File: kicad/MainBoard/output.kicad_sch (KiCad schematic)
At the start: 124 parts, among them J11 CHAN1, J12 CHAN2, J13 Conn_01x02, J14 CHAN3, J15 CHAN4, Q10 AO3400A, Q11 AO3400A, Q12 IRF9Z24NPBF, Q13 AO3400A, Q18 AO3401A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

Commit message: update out of stock 0.5R resistor C705591 to be C175573 instead
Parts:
- R36, R61: LCSC C705591 -> C175573
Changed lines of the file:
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@@
       (effects (font (size 1.27 1.27)) hide)
     )
-    (property "LCSC" "C705591" (id 4) (at 105.41 109.855 90)
+    (property "LCSC" "C175573" (id 4) (at 105.41 109.855 90)
       (effects (font (size 1.27 1.27)) hide)
     )
@@
       (effects (font (size 1.27 1.27)) hide)
     )
-    (property "LCSC" "C705591" (id 4) (at 105.41 17.145 90)
-      (effects (font (size 1.27 1.27)) hide)
-    )
+    (property "LCSC" "C175573" (id 4) (at 105.41 17.145 90)
+      (effects (font (size 1.27 1.27)) hide)
+    )

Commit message: Add PCB v2.3 kicad project files + gerbers
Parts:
- J13: footprint Connector_PinHeader_2.54mm:PinHeader_1x02_P2.54mm_Vertical -> Connector_Molex:Molex_KK-254_AE-6410-02A_1x02_P2.54mm_Vertical
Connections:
- net GND: now also J13.2 (Pin_2); no longer J13.1 (Pin_1)
- net SERIAL_TX: now also J13.1 (Pin_1); no longer J13.2 (Pin_2)
- net 4v renamed 3.5v
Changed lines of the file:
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@@
   (junction (at 128.27 180.975) (diameter 0) (color 0 0 0 0)
   )
+  (junction (at 84.455 210.185) (diameter 0) (color 0 0 0 0)
+  )
   (junction (at 118.11 161.925) (diameter 0) (color 0 0 0 0)
   )
@@
   (junction (at 128.27 81.915) (diameter 0) (color 0 0 0 0)
   )
-  (junction (at 84.455 210.185) (diameter 0) (color 0 0 0 0)
-  )
   (junction (at 36.83 85.725) (diameter 0) (color 0 0 0 0)
   )
@@
     (stroke (width 0) (type default) (color 0 0 0 0))
   )
+  (wire (pts (xy 81.28 210.185) (xy 84.455 210.185))
+    (stroke (width 0) (type default) (color 0 0 0 0))
+  )
   (wire (pts (xy 92.71 121.285) (xy 92.71 135.255))
     (stroke (width 0) (type default) (color 0 0 0 0))
@@
     (stroke (width 0) (type default) (color 0 0 0 0))
   )
-  (wire (pts (xy 82.55 210.185) (xy 84.455 210.185))
-    (stroke (width 0) (type default) (color 0 0 0 0))
-  )
   (wire (pts (xy 154.94 175.895) (xy 154.94 183.515))
     (stroke (width 0) (type default) (color 0 0 0 0))
@@
     (stroke (width 0) (type default) (color 0 0 0 0))
   )
+  (wire (pts (xy 81.28 210.185) (xy 81.28 210.82))
+    (stroke (width 0) (type default) (color 0 0 0 0))
+  )
   (polyline (pts (xy 76.2 198.12) (xy 76.2 266.7))
     (stroke (width 0) (type default) (color 0 0 0 0))
@@
     (stroke (width 0) (type default) (color 0 0 0 0))
   )
-  (wire (pts (xy 84.455 210.185) (xy 88.265 210.185))
-    (stroke (width 0) (type default) (color 0 0 0 0))
-  )
   (wire (pts (xy 154.94 47.625) (xy 185.42 47.625))
     (stroke (width 0) (type default) (color 0 0 0 0))
@@
     (stroke (width 0) (type default) (color 0 0 0 0))
   )
+  (wire (pts (xy 84.455 210.185) (xy 88.265 210.185))
+    (stroke (width 0) (type default) (color 0 0 0 0))
+  )
   (wire (pts (xy 76.2 179.705) (xy 76.2 186.055))
     (stroke (width 0) (type default) (color 0 0 0 0))
@@
     (effects (font (size 1.27 1.27)) (justify right))
   )
-  (hierarchical_label "4v" (shape input) (at 82.55 210.185 180)
+  (hierarchical_label "3.5v" (shape input) (at 81.28 210.82 270)
     (effects (font (size 1.27 1.27)) (justify right))
   )
@@
     (effects (font (size 1.27 1.27)) (justify left))
   )
-  (hierarchical_label "4v" (shape input) (at 63.5 201.295 180)
+  (hierarchical_label "3.5v" (shape input) (at 63.5 201.295 180)
     (effects (font (size 1.27 1.27)) (justify right))
   )
@@
     (pin "2")
   )
-  (symbol (lib_id "Connector_Generic:Conn_01x02") (at 39.37 145.415 0) (unit 1)
-    (in_bom yes) (on_board yes) (fields_autoplaced)
-    (property "Reference" "J13" (id 0) (at 41.402 145.8503 0)
-      (effects (font (size 1.27 1.27)) (justify left))
-    )
-    (property "Value" "Conn_01x02" (id 1) (at 41.402 148.3872 0)
-      (effects (font (size 1.27 1.27)) (justify left))
-    )
-    (property "Footprint" "Connector_PinHeader_2.54mm:PinHeader_1x02_P2.54mm_Vertical" (id 2) (at 39.37 145.415 0)
+  (symbol (lib_id "Connector_Generic:Conn_01x02") (at 39.37 147.955 0) (mirror x) (unit 1)
+    (in_bom yes) (on_board yes)
+    (property "Reference" "J13" (id 0) (at 39.37 151.13 0))
+    (property "Value" "Conn_01x02" (id 1) (at 39.37 142.9821 0))
+    (property "Footprint" "Connector_Molex:Molex_KK-254_AE-6410-02A_1x02_P2.54mm_Vertical" (id 2) (at 39.37 147.955 0)
       (effects (font (size 1.27 1.27)) hide)
     )
-    (property "Datasheet" "~" (id 3) (at 39.37 145.415 0)
+    (property "Datasheet" "~" (id 3) (at 39.37 147.955 0)
       (effects (font (size 1.27 1.27)) hide)
     )
-    (property "LCSC" "C27543" (id 4) (at 39.37 145.415 0)
+    (property "LCSC" "C27543" (id 4) (at 39.37 147.955 0)
       (effects (font (size 1.27 1.27)) hide)
     )

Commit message: Mainboard PCB v2.4
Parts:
- added R152: 10k, Resistor_SMD:R_0603_1608Metric_Pad0.98x0.95mm_HandSolder, symbol Device:R_Small
- R36, R61: footprint Resistor_SMD:R_1218_3246Metric_Pad1.22x4.75mm_HandSolder -> Resistor_SMD:R_2512_6332Metric_Pad1.40x3.35mm_HandSolder; LCSC C175573 -> C2904268
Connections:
- net 9v_EN: now also R152.1
- net GND: now also R152.2
- net at J12.R: now also J12.S, TR2.4
- net at J15.R: now also J15.S, TR4.4
- net at J14.R: now also J14.S, TR3.4
- net at J11.R: now also J11.S, TR1.4
- net PWR_EN: now reaches U9.37 (3V3_EN)
- no-connect marks 26 -> 21
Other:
- moved on the sheet: C28, C29

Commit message: v2.5 schematic + PCB changes
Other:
- company: (none) -> CrashOverride85
- title: (none) -> ZC95 MKII
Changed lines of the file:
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@@
 (kicad_sch (version 20211123) (generator eeschema)
   (paper "A4" portrait)
+  (title_block
+    (title "ZC95 MKII")
+    (rev "2.5")
+    (company "CrashOverride85")
+  )
   (junction (at 128.27 45.085) (diameter 0) (color 0 0 0 0)
   )

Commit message: tweaks
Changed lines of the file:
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@@
   (symbol (lib_id "Device:R_Small") (at 92.71 26.035 180) (unit 1)
     (in_bom yes) (on_board yes)
-    (property "Reference" "R37" (id 0) (at 88.9 26.035 0)
+    (property "Reference" "R37" (id 0) (at 86.995 26.035 0)
       (effects (font (size 1.27 1.27)) (justify right))
     )

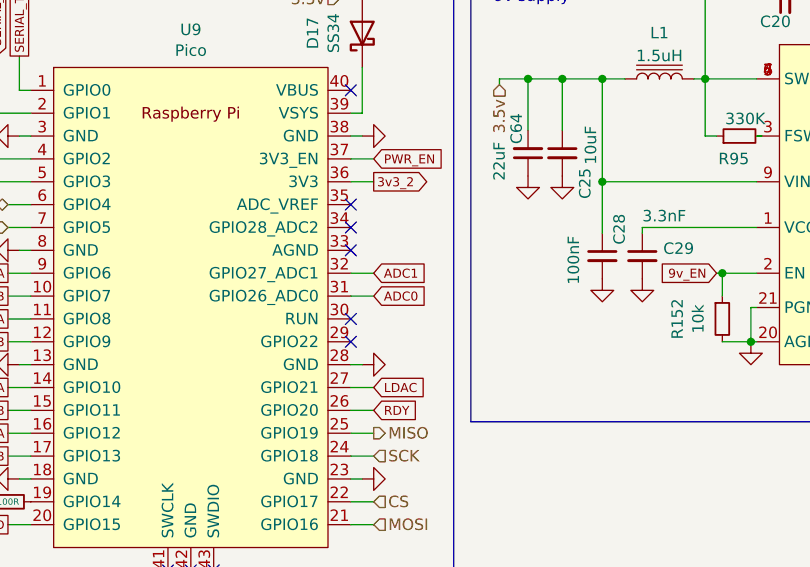
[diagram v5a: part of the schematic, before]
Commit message: v2.6 schematic + pcb changes
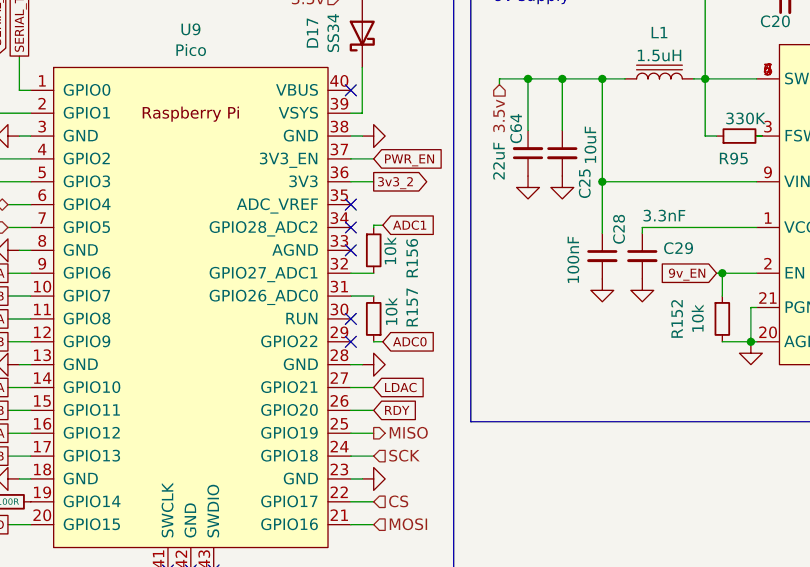
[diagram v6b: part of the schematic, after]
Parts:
- added R156, R157: 10k, Resistor_SMD:R_0603_1608Metric_Pad0.98x0.95mm_HandSolder, symbol Device:R_Small
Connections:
- net ADC0: now also R157.1; no longer U9.31 (GPIO26_ADC0)
- net ADC1: now also R156.1; no longer U9.32 (GPIO27_ADC1)
- new net: R157.2, U9.31 (GPIO26_ADC0)
- new net: R156.2, U9.32 (GPIO27_ADC1)
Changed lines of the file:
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@@
+    (stroke (width 0) (type default) (color 0 0 0 0))
+  )
+  (wire (pts (xy 67.31 226.441) (xy 67.31 226.695))
     (stroke (width 0) (type default) (color 0 0 0 0))
   )
@@
     (stroke (width 0) (type default) (color 0 0 0 0))
   )
+  (wire (pts (xy 68.326 226.441) (xy 67.31 226.441))
+    (stroke (width 0) (type default) (color 0 0 0 0))
+  )
   (wire (pts (xy 183.515 234.95) (xy 179.705 234.95))
     (stroke (width 0) (type default) (color 0 0 0 0))
@@
   )
   (wire (pts (xy 154.94 183.515) (xy 135.89 183.515))
+    (stroke (width 0) (type default) (color 0 0 0 0))
+  )
+  (wire (pts (xy 67.31 239.395) (xy 68.326 239.395))
     (stroke (width 0) (type default) (color 0 0 0 0))
   )
@@
     )
   )
-  (global_label "ADC0" (shape input) (at 67.31 234.315 0) (fields_autoplaced)
+  (global_label "ADC0" (shape input) (at 68.326 239.395 0) (fields_autoplaced)
     (effects (font (size 1 1)) (justify left))
-    (property "Intersheet References" "${INTERSHEET_REFS}" (id 0) (at 73.0195 234.2525 0)
+    (property "Intersheet References" "${INTERSHEET_REFS}" (id 0) (at 74.0355 239.3325 0)
       (effects (font (size 1 1)) (justify left) hide)
     )
@@
     )
   )
-  (global_label "ADC1" (shape input) (at 67.31 231.775 0) (fields_autoplaced)
+  (global_label "ADC1" (shape input) (at 68.326 226.441 0) (fields_autoplaced)
     (effects (font (size 1 1)) (justify left))
-    (property "Intersheet References" "${INTERSHEET_REFS}" (id 0) (at 73.0195 231.7125 0)
+    (property "Intersheet References" "${INTERSHEET_REFS}" (id 0) (at 74.0355 226.3785 0)
       (effects (font (size 1 1)) (justify left) hide)
     )
@@
     )
     (pin "1")
+  )
+  (symbol (lib_id "Device:R_Small") (at 67.31 236.855 180) (unit 1)
+    (in_bom yes) (on_board yes)
+    (property "Reference" "R157" (id 0) (at 71.628 235.585 90))
+    (property "Value" "10k" (id 1) (at 69.342 236.093 90))
+    (property "Footprint" "Resistor_SMD:R_0603_1608Metric_Pad0.98x0.95mm_HandSolder" (id 2) (at 67.31 236.855 0)
+      (effects (font (size 1.27 1.27)) hide)
+    )
+    (property "Datasheet" "~" (id 3) (at 67.31 236.855 0)
+      (effects (font (size 1.27 1.27)) hide)
+    )
+    (property "LCSC" "C25804" (id 4) (at 67.31 236.855 90)
+      (effects (font (size 1.27 1.27)) hide)
+    )
+    (pin "1")
+    (pin "2")
   )
   (symbol (lib_id "Amplifier_Operational:LM324") (at 27.94 88.265 270) (unit 5)
@@
     (pin "1")
   )
+  (symbol (lib_id "Device:R_Small") (at 67.31 229.235 0) (unit 1)
+    (in_bom yes) (on_board yes)
+    (property "Reference" "R156" (id 0) (at 71.628 230.124 90))
+    (property "Value" "10k" (id 1) (at 69.215 229.362 90))
+    (property "Footprint" "Resistor_SMD:R_0603_1608Metric_Pad0.98x0.95mm_HandSolder" (id 2) (at 67.31 229.235 0)
+      (effects (font (size 1.27 1.27)) hide)
+    )
+    (property "Datasheet" "~" (id 3) (at 67.31 229.235 0)
+      (effects (font (size 1.27 1.27)) hide)
+    )
+    (property "LCSC" "C25804" (id 4) (at 67.31 229.235 90)
+      (effects (font (size 1.27 1.27)) hide)
+    )
+    (pin "1")
+    (pin "2")
+  )
   (symbol (lib_id "power:GND") (at 141.605 215.9 0) (unit 1)
